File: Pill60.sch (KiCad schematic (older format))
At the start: 139 parts, among them J1 OLED, SW1 Rotary_Encoder_Switch, U1 ChinaBluePill

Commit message: gerber
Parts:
- added H1, H2, H3, H4, H5, H6, H7: Hole, MountingHole:MountingHole_2.2mm_M2, symbol keebio:Hole
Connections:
- no-connect marks 0 -> 11
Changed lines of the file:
@@
-$EndComp
-$Comp
-L MX_Alps_Hybrid:MX-NoLED MXBSPC1
-U 1 1 5F3D669D
-P 9250 3500
-F 0 "MXBSPC1" H 9283 3723 60  0000 C CNN
-F 1 "MX-NoLED" H 9283 3649 20  0000 C CNN
-F 2 "MX_Only:MXOnly-1U-Hotswap-Antishear" H 8625 3475 60  0001 C CNN
-F 3 "" H 8625 3475 60  0001 C CNN
-	1    9250 3500
-	1    0    0    -1
 $EndComp
 $Comp
@@
 $EndComp
 $Comp
-L MX_Alps_Hybrid:MX-NoLED 15MXBSLSH1
-U 1 1 5F53A61E
-P 9250 4450
-F 0 "15MXBSLSH1" H 9283 4673 60  0000 C CNN
-F 1 "MX-NoLED" H 9283 4599 20  0000 C CNN
-F 2 "MX_Only:MXOnly-1.5U-Hotswap-AntiShear" H 8625 4425 60  0001 C CNN
-F 3 "" H 8625 4425 60  0001 C CNN
-	1    9250 4450
-	1    0    0    -1
-$EndComp
-$Comp
 L MX_Alps_Hybrid:MX-NoLED MXFN1
 U 1 1 5F53A62A
@@
 $EndComp
 $Comp
-L MX_Alps_Hybrid:MX-NoLED MXDEL1
-U 1 1 5F53A636
-P 9250 5200
-F 0 "MXDEL1" H 9283 5423 60  0000 C CNN
-F 1 "MX-NoLED" H 9283 5349 20  0000 C CNN
-F 2 "MX_Only:MXOnly-1U-Hotswap-Antishear" H 8625 5175 60  0001 C CNN
-F 3 "" H 8625 5175 60  0001 C CNN
-	1    9250 5200
-	1    0    0    -1
-$EndComp
-$Comp
 L MX_Alps_Hybrid:MX-NoLED 15MXLCTRL1
 U 1 1 5F544C28
@@
 $EndComp
 $Comp
-L Diode:1N4148W D58
-U 1 1 5F4616B7
-P 9200 3800
-F 0 "D58" V 9246 3720 50  0000 R CNN
-F 1 "1N4148W" V 9155 3720 50  0000 R CNN
-F 2 "Diode_SMD:D_SOD-123" H 9200 3625 50  0001 C CNN
-F 3 "https://www.vishay.com/docs/85748/1n4148w.pdf" H 9200 3800 50  0001 C CNN
-	1    9200 3800
-	0    -1   -1   0
-$EndComp
-$Comp
 L Diode:1N4148W D7
 U 1 1 5F47AC29
@@
 $EndComp
 $Comp
-L Diode:1N4148W D59
-U 1 1 5F47AC77
-P 9200 4750
-F 0 "D59" V 9246 4670 50  0000 R CNN
-F 1 "1N4148W" V 9155 4670 50  0000 R CNN
-F 2 "Diode_SMD:D_SOD-123" H 9200 4575 50  0001 C CNN
-F 3 "https://www.vishay.com/docs/85748/1n4148w.pdf" H 9200 4750 50  0001 C CNN
-	1    9200 4750
-	0    -1   -1   0
-$EndComp
-$Comp
 L Diode:1N4148W D8
 U 1 1 5F48F64C
@@
 $EndComp
 $Comp
-L Diode:1N4148W D63
-U 1 1 5F48F694
-P 9200 5500
-F 0 "D63" V 9246 5420 50  0000 R CNN
-F 1 "1N4148W" V 9155 5420 50  0000 R CNN
-F 2 "Diode_SMD:D_SOD-123" H 9200 5325 50  0001 C CNN
-F 3 "https://www.vishay.com/docs/85748/1n4148w.pdf" H 9200 5500 50  0001 C CNN
-	1    9200 5500
-	0    -1   -1   0
-$EndComp
-$Comp
 L Diode:1N4148W D60
 U 1 1 5F48F69A
@@
 Wire Wire Line
 	8800 6800 8800 7600
-Wire Wire Line
-	9400 3000 9400 3450
-Connection ~ 9400 3450
-Wire Wire Line
-	9400 3450 9400 4400
-Connection ~ 9400 4400
 Connection ~ 9400 6800
 Wire Wire Line
 	9400 6800 9400 7600
-Wire Wire Line
-	9200 3950 8600 3950
 Connection ~ 2600 3950
 Wire Wire Line
@@
 Wire Wire Line
 	8050 3950 7500 3950
-Connection ~ 8600 3950
 Wire Wire Line
 	8600 3950 8050 3950
@@
 Wire Wire Line
 	8050 4900 8600 4900
-Connection ~ 8600 4900
-Wire Wire Line
-	8600 4900 9200 4900
 Wire Wire Line
 	1500 5650 2600 5650
@@
 Wire Wire Line
 	8050 5650 8600 5650
-Connection ~ 8600 5650
-Wire Wire Line
-	8600 5650 9200 5650
 Wire Wire Line
 	1500 6450 2600 6450
@@
 	8800 5950 8800 6800
 Connection ~ 8800 5950
-Connection ~ 9400 5150
 Wire Wire Line
 	9200 7300 8600 7300
@@
 Text GLabel 5550 1750 2    50   Input ~ 0
 SWE2
-Text GLabel 4200 6700 0    50   Input ~ 0
-SWE1
-Text GLabel 4000 7000 1    50   Input ~ 0
-SWE2
-$Comp
-L Diode:1N4148W D64
-U 1 1 5F3FC91B
-P 4000 7150
-F 0 "D64" V 4046 7070 50  0000 R CNN
-F 1 "1N4148W" V 3955 7070 50  0000 R CNN
-F 2 "Diode_SMD:D_SOD-123" H 4000 6975 50  0001 C CNN
-F 3 "https://www.vishay.com/docs/85748/1n4148w.pdf" H 4000 7150 50  0001 C CNN
-	1    4000 7150
-	0    -1   -1   0
-$EndComp
-Wire Wire Line
-	9400 4400 9400 5150
-Wire Wire Line
-	3500 7300 4000 7300
 Text GLabel 11700 2000 0    50   Input ~ 0
 COL4
@@
 Text GLabel 13100 2400 2    50   Input ~ 0
 ROW0
-Connection ~ 4000 7300
-Wire Wire Line
-	4000 7300 5500 7300
-Wire Wire Line
-	4200 5950 4200 6700
-Connection ~ 4200 5950
-Wire Wire Line
-	9400 5150 9400 6800
 $Comp
 L china_bluepill:ChinaBluePill U1
@@
 Text GLabel 13100 2500 2    50   Input ~ 0
 COL0
+Connection ~ 4200 5950
+Wire Wire Line
+	4200 5950 4200 6700
+Connection ~ 4000 7300
+Wire Wire Line
+	4000 7300 5500 7300
+Wire Wire Line
+	3500 7300 4000 7300
+$Comp
+L Diode:1N4148W D64
+U 1 1 5F3FC91B
+P 4000 7150
+F 0 "D64" V 4046 7070 50  0000 R CNN
+F 1 "1N4148W" V 3955 7070 50  0000 R CNN
+F 2 "Diode_SMD:D_SOD-123" H 4000 6975 50  0001 C CNN
+F 3 "https://www.vishay.com/docs/85748/1n4148w.pdf" H 4000 7150 50  0001 C CNN
+	1    4000 7150
+	0    -1   -1   0
+$EndComp
+Text GLabel 4000 7000 1    50   Input ~ 0
+SWE2
+Text GLabel 4200 6700 0    50   Input ~ 0
+SWE1
+Wire Wire Line
+	9400 4400 9400 5150
+Connection ~ 9400 5150
+Connection ~ 8600 5650
+Connection ~ 8600 4900
+Connection ~ 8600 3950
+Connection ~ 9400 4400
+Connection ~ 9400 3450
+Wire Wire Line
+	9400 3000 9400 3450
+Wire Wire Line
+	9400 5150 9400 6800
+Wire Wire Line
+	9400 3450 9400 4400
+Wire Wire Line
+	8600 5650 9200 5650
+Wire Wire Line
+	8600 4900 9200 4900
+Wire Wire Line
+	9200 3950 8600 3950
+$Comp
+L Diode:1N4148W D63
+U 1 1 5F48F694
+P 9200 5500
+F 0 "D63" V 9246 5420 50  0000 R CNN
+F 1 "1N4148W" V 9155 5420 50  0000 R CNN
+F 2 "Diode_SMD:D_SOD-123" H 9200 5325 50  0001 C CNN
+F 3 "https://www.vishay.com/docs/85748/1n4148w.pdf" H 9200 5500 50  0001 C CNN
+	1    9200 5500
+	0    -1   -1   0
+$EndComp
+$Comp
+L Diode:1N4148W D59
+U 1 1 5F47AC77
+P 9200 4750
+F 0 "D59" V 9246 4670 50  0000 R CNN
+F 1 "1N4148W" V 9155 4670 50  0000 R CNN
+F 2 "Diode_SMD:D_SOD-123" H 9200 4575 50  0001 C CNN
+F 3 "https://www.vishay.com/docs/85748/1n4148w.pdf" H 9200 4750 50  0001 C CNN
+	1    9200 4750
+	0    -1   -1   0
+$EndComp
+$Comp
+L Diode:1N4148W D58
+U 1 1 5F4616B7
+P 9200 3800
+F 0 "D58" V 9246 3720 50  0000 R CNN
+F 1 "1N4148W" V 9155 3720 50  0000 R CNN
+F 2 "Diode_SMD:D_SOD-123" H 9200 3625 50  0001 C CNN
+F 3 "https://www.vishay.com/docs/85748/1n4148w.pdf" H 9200 3800 50  0001 C CNN
+	1    9200 3800
+	0    -1   -1   0
+$EndComp
+$Comp
+L MX_Alps_Hybrid:MX-NoLED MXDEL1
+U 1 1 5F53A636
+P 9250 5200
+F 0 "MXDEL1" H 9283 5423 60  0000 C CNN
+F 1 "MX-NoLED" H 9283 5349 20  0000 C CNN
+F 2 "MX_Only:MXOnly-1U-Hotswap-Antishear" H 8625 5175 60  0001 C CNN
+F 3 "" H 8625 5175 60  0001 C CNN
+	1    9250 5200
+	1    0    0    -1
+$EndComp
+$Comp
+L MX_Alps_Hybrid:MX-NoLED 15MXBSLSH1
+U 1 1 5F53A61E
+P 9250 4450
+F 0 "15MXBSLSH1" H 9283 4673 60  0000 C CNN
+F 1 "MX-NoLED" H 9283 4599 20  0000 C CNN
+F 2 "MX_Only:MXOnly-1.5U-Hotswap-AntiShear" H 8625 4425 60  0001 C CNN
+F 3 "" H 8625 4425 60  0001 C CNN
+	1    9250 4450
+	1    0    0    -1
+$EndComp
+$Comp
+L MX_Alps_Hybrid:MX-NoLED MXBSPC1
+U 1 1 5F3D669D
+P 9250 3500
+F 0 "MXBSPC1" H 9283 3723 60  0000 C CNN
+F 1 "MX-NoLED" H 9283 3649 20  0000 C CNN
+F 2 "MX_Only:MXOnly-1U-Hotswap-Antishear" H 8625 3475 60  0001 C CNN
+F 3 "" H 8625 3475 60  0001 C CNN
+	1    9250 3500
+	1    0    0    -1
+$EndComp
+$Comp
+L keebio:Hole H1
+U 1 1 5F48208A
+P 11150 5500
+F 0 "H1" H 11336 5553 60  0000 L CNN
+F 1 "Hole" H 11336 5447 60  0000 L CNN
+F 2 "MountingHole:MountingHole_2.2mm_M2" H 11150 5500 60  0001 C CNN
+F 3 "" H 11150 5500 60  0001 C CNN
+	1    11150 5500
+	1    0    0    -1
+$EndComp
+$Comp
+L keebio:Hole H2
+U 1 1 5F4826F6
+P 11800 5500
+F 0 "H2" H 11986 5553 60  0000 L CNN
+F 1 "Hole" H 11986 5447 60  0000 L CNN
+F 2 "MountingHole:MountingHole_2.2mm_M2" H 11800 5500 60  0001 C CNN
+F 3 "" H 11800 5500 60  0001 C CNN
+	1    11800 5500
+	1    0    0    -1
+$EndComp
+$Comp
+L keebio:Hole H3
+U 1 1 5F482881
+P 12400 5500
+F 0 "H3" H 12586 5553 60  0000 L CNN
+F 1 "Hole" H 12586 5447 60  0000 L CNN
+F 2 "MountingHole:MountingHole_2.2mm_M2" H 12400 5500 60  0001 C CNN
+F 3 "" H 12400 5500 60  0001 C CNN
+	1    12400 5500
+	1    0    0    -1
+$EndComp
+$Comp
+L keebio:Hole H4
+U 1 1 5F482A97
+P 12950 5500
+F 0 "H4" H 13136 5553 60  0000 L CNN
+F 1 "Hole" H 13136 5447 60  0000 L CNN
+F 2 "MountingHole:MountingHole_2.2mm_M2" H 12950 5500 60  0001 C CNN
+F 3 "" H 12950 5500 60  0001 C CNN
+	1    12950 5500
+	1    0    0    -1
+$EndComp
+$Comp
+L keebio:Hole H5
+U 1 1 5F482CBA
+P 13500 5500
+F 0 "H5" H 13686 5553 60  0000 L CNN
+F 1 "Hole" H 13686 5447 60  0000 L CNN
+F 2 "MountingHole:MountingHole_2.2mm_M2" H 13500 5500 60  0001 C CNN
+F 3 "" H 13500 5500 60  0001 C CNN
+	1    13500 5500
+	1    0    0    -1
+$EndComp
+$Comp
+L keebio:Hole H6
+U 1 1 5F482E8A
+P 14050 5500
+F 0 "H6" H 14236 5553 60  0000 L CNN
+F 1 "Hole" H 14236 5447 60  0000 L CNN
+F 2 "MountingHole:MountingHole_2.2mm_M2" H 14050 5500 60  0001 C CNN
+F 3 "" H 14050 5500 60  0001 C CNN
+	1    14050 5500
+	1    0    0    -1
+$EndComp
+$Comp
+L keebio:Hole H7
+U 1 1 5F483003
+P 14650 5500
+F 0 "H7" H 14836 5553 60  0000 L CNN
+F 1 "Hole" H 14836 5447 60  0000 L CNN
+F 2 "MountingHole:MountingHole_2.2mm_M2" H 14650 5500 60  0001 C CNN
+F 3 "" H 14650 5500 60  0001 C CNN
+	1    14650 5500
+	1    0    0    -1
+$EndComp
+NoConn ~ 11700 2800
+NoConn ~ 11700 2900
+NoConn ~ 11700 3000
+NoConn ~ 11700 3100
+NoConn ~ 11700 3400
+NoConn ~ 11700 3500
+NoConn ~ 13100 3300
+NoConn ~ 13100 3400
+NoConn ~ 13100 3500
+NoConn ~ 13100 3600
+NoConn ~ 13100 3700
 $EndSCHEMATC

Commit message: add underglow
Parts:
- added L0, L1, L10, L11, L12, L13, L2, L3, L4, L5, L6, L7, L8, L9: SK6812MINI, LED_SMD:LED_SK6812MINI_PLCC4_3.5x3.5mm_P1.75mm, symbol LED:SK6812MINI
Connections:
- net +5V: now also L0.4 (VDD), L1.4 (VDD), L10.4 (VDD), L11.4 (VDD), L12.4 (VDD), L13.4 (VDD), L2.4 (VDD), L3.4 (VDD), L4.4 (VDD), L5.4 (VDD), L6.4 (VDD), L7.4 (VDD), L8.4 (VDD), L9.4 (VDD)
- net GND: now also L0.2 (VSS), L1.2 (VSS), L10.2 (VSS), L11.2 (VSS), L12.2 (VSS), L13.2 (VSS), L2.2 (VSS), L3.2 (VSS), L4.2 (VSS), L5.2 (VSS), L6.2 (VSS), L7.2 (VSS), L8.2 (VSS), L9.2 (VSS)
- net LED: now reaches U1.PA9
- net LED: now also L0.3 (DIN)
- new net: L0.1 (DOUT), L1.3 (DIN)
- new net: L1.1 (DOUT), L2.3 (DIN)
- new net: L2.1 (DOUT), L3.3 (DIN)
- new net: L3.1 (DOUT), L4.3 (DIN)
- new net: L7.1 (DOUT), L8.3 (DIN)
- new net: L6.1 (DOUT), L7.3 (DIN)
- new net: L5.1 (DOUT), L6.3 (DIN)
- new net: L4.1 (DOUT), L5.3 (DIN)
- new net: L12.1 (DOUT), L13.3 (DIN)
- new net: L11.1 (DOUT), L12.3 (DIN)
- new net: L10.3 (DIN), L9.1 (DOUT)
- new net: L8.1 (DOUT), L9.3 (DIN)
- new net: L10.1 (DOUT), L11.3 (DIN)
- no-connect marks 11 -> 10
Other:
- moved on the sheet: H1, H2, H3, H4, H5, H6, H7

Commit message: Fix wires and make stuff better
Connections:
- net COL0: now also U1.PB7; no longer U1.PB6
- net COL1: now also U1.PB8; no longer U1.PB7
- net COL2: now also U1.PB9; no longer U1.PB8
- net COL3: now also U1.PB6; no longer U1.PB9
- net ENCA: now also U1.PB13; no longer U1.PB12
- net ENCB: now also U1.PB12; no longer U1.PB13
- net ROW0: now also U1.PB4; no longer U1.PB5
- net ROW1: now also U1.PB3; no longer U1.PB4
- net ROW2: now also U1.PA15; no longer U1.PB3
- net ROW3: now also U1.PA12; no longer U1.PA15
- net ROW4: now also U1.PB5; no longer U1.PA12
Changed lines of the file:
@@
 Text GLabel 4950 1750 0    50   Input ~ 0
 ENCB
+Text GLabel 13100 3200 2    50   Input ~ 0
+ENCA
 Text GLabel 13100 3100 2    50   Input ~ 0
-ENCA
-Text GLabel 13100 3200 2    50   Input ~ 0
 ENCB
 $Comp
@@
 	0    -1   -1   0
 $EndComp
+Text GLabel 13100 2400 2    50   Input ~ 0
+ROW4
 Text GLabel 11700 3200 0    50   Input ~ 0
-ROW4
+ROW3
 Text GLabel 11700 3300 0    50   Input ~ 0
-ROW3
+ROW2
 Text GLabel 13100 2200 2    50   Input ~ 0
-ROW2
-Text GLabel 13100 2300 2    50   Input ~ 0
 ROW1
 $Comp
@@
 	1    0    0    -1
 $EndComp
+Text GLabel 13100 2500 2    50   Input ~ 0
+COL3
 Text GLabel 13100 2800 2    50   Input ~ 0
-COL3
+COL2
 Text GLabel 13100 2700 2    50   Input ~ 0
-COL2
-Text GLabel 13100 2600 2    50   Input ~ 0
 COL1
 Connection ~ 4200 5950
@@
 NoConn ~ 13100 3600
 NoConn ~ 13100 3700
-Text GLabel 13100 2500 2    50   Input ~ 0
+Text GLabel 13100 2600 2    50   Input ~ 0
 COL0
-Text GLabel 13100 2400 2    50   Input ~ 0
+Text GLabel 13100 2300 2    50   Input ~ 0
 ROW0
 Text GLabel 11700 2900 0    50   Input ~ 0

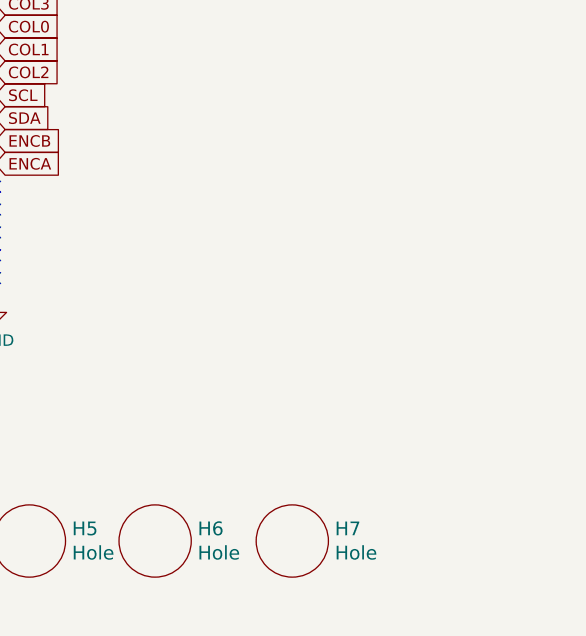
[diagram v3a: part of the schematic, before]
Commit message: added more holes for plate and pcb mounting
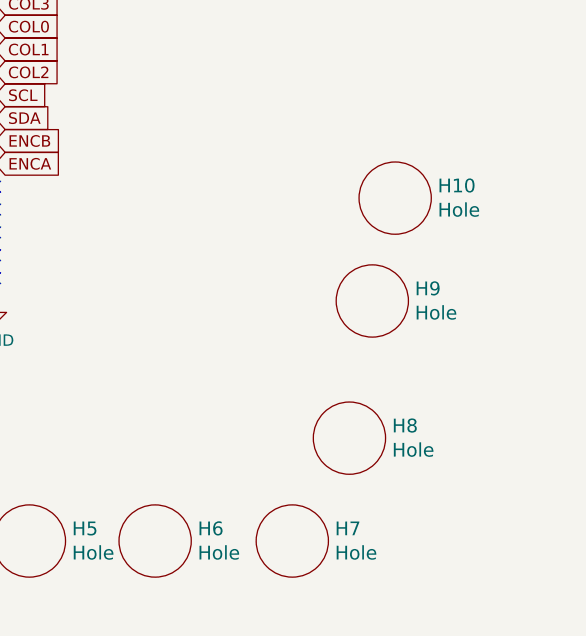
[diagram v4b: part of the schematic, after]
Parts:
- added H10, H8, H9: Hole, MountingHole:MountingHole_2.2mm_M2, symbol keebio:Hole
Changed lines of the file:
@@
 Wire Wire Line
 	10300 8150 13300 8150
+$Comp
+L keebio:Hole H8
+U 1 1 5F429E69
+P 14650 4400
+F 0 "H8" H 14836 4453 60  0000 L CNN
+F 1 "Hole" H 14836 4347 60  0000 L CNN
+F 2 "MountingHole:MountingHole_2.2mm_M2" H 14650 4400 60  0001 C CNN
+F 3 "" H 14650 4400 60  0001 C CNN
+	1    14650 4400
+	1    0    0    -1
+$EndComp
+$Comp
+L keebio:Hole H9
+U 1 1 5F42A107
+P 14750 3800
+F 0 "H9" H 14936 3853 60  0000 L CNN
+F 1 "Hole" H 14936 3747 60  0000 L CNN
+F 2 "MountingHole:MountingHole_2.2mm_M2" H 14750 3800 60  0001 C CNN
+F 3 "" H 14750 3800 60  0001 C CNN
+	1    14750 3800
+	1    0    0    -1
+$EndComp
+$Comp
+L keebio:Hole H10
+U 1 1 5F42A374
+P 14850 3350
+F 0 "H10" H 15036 3403 60  0000 L CNN
+F 1 "Hole" H 15036 3297 60  0000 L CNN
+F 2 "MountingHole:MountingHole_2.2mm_M2" H 14850 3350 60  0001 C CNN
+F 3 "" H 14850 3350 60  0001 C CNN
+	1    14850 3350
+	1    0    0    -1
+$EndComp
 $EndSCHEMATC

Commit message: Sneaky footprint
offset pin holes for bluepill, might or might not work
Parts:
- U1: footprint chinabluepill:ChinaBluePill -> chinabluepill:ChinaBluePill_SneakyFootprint
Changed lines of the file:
@@
 F 0 "U1" H 12400 3365 50  0000 C CNN
 F 1 "ChinaBluePill" H 12400 3274 50  0000 C CNN
-F 2 "chinabluepill:ChinaBluePill" H 12400 2550 50  0001 C CNN
+F 2 "chinabluepill:ChinaBluePill_SneakyFootprint" H 12400 2550 50  0001 C CNN
 F 3 "" H 12400 2550 50  0001 C CNN
 	1    12400 2550

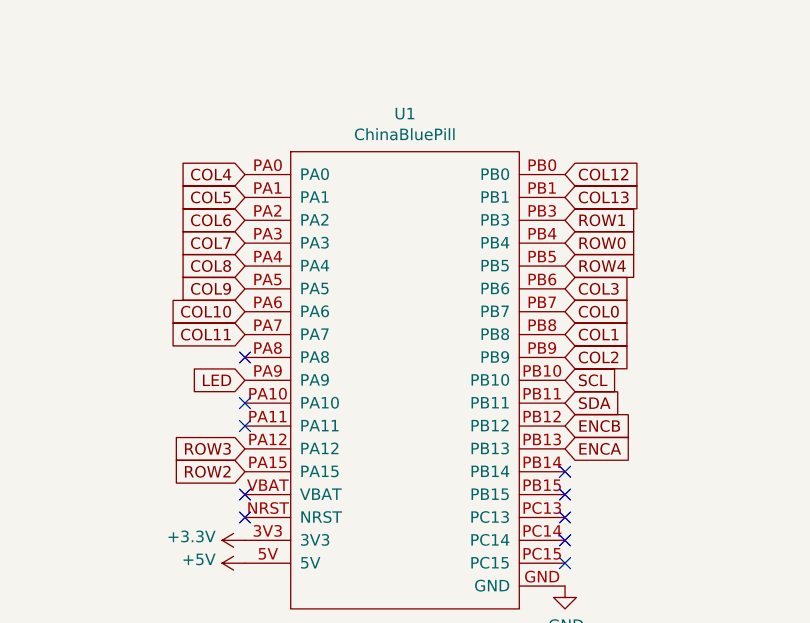
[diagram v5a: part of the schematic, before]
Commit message: added support for blackpill
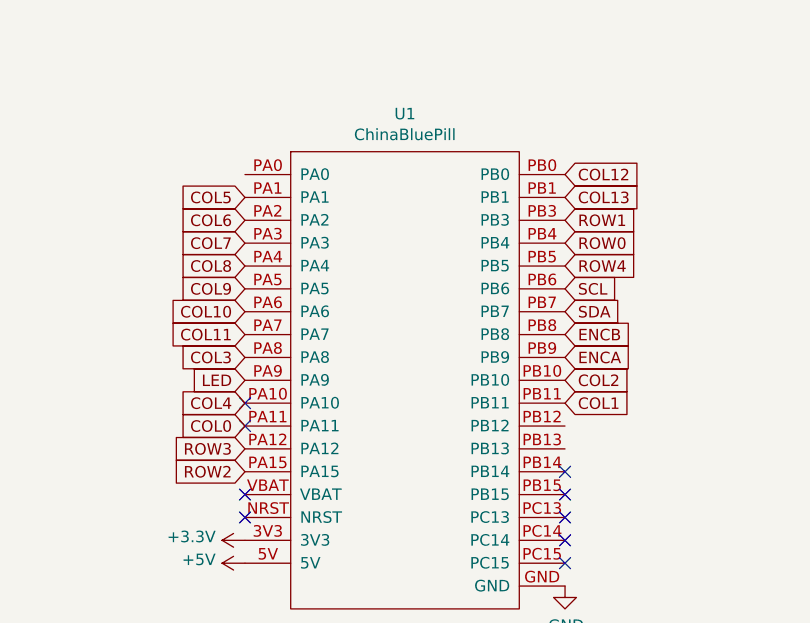
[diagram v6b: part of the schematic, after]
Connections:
- net COL0: now also U1.PA11; no longer U1.PB7
- net COL1: now also U1.PB11; no longer U1.PB8
- net COL2: now also U1.PB10; no longer U1.PB9
- net COL3: now also U1.PA8; no longer U1.PB6
- net COL4: now also U1.PA10; no longer U1.PA0
- net ENCA: now also U1.PB9; no longer U1.PB13
- net ENCB: now also U1.PB8; no longer U1.PB12
- net SCL: now also U1.PB6; no longer U1.PB10
- net SDA: now also U1.PB7; no longer U1.PB11
- no-connect marks 10 -> 9
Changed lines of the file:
@@
 	1    0    0    -1
 $EndComp
-Text GLabel 13100 3000 2    50   Input ~ 0
+Text GLabel 13100 2600 2    50   Input ~ 0
 SDA
-Text GLabel 13100 2900 2    50   Input ~ 0
+Text GLabel 13100 2500 2    50   Input ~ 0
 SCL
 $Comp
@@
 Text GLabel 5550 1750 2    50   Input ~ 0
 SWE2
-Text GLabel 11700 2000 0    50   Input ~ 0
+Text GLabel 11700 3000 0    50   Input ~ 0
 COL4
 Text GLabel 11700 2100 0    50   Input ~ 0
@@
 Text GLabel 4950 1750 0    50   Input ~ 0
 ENCB
-Text GLabel 13100 3200 2    50   Input ~ 0
+Text GLabel 13100 2800 2    50   Input ~ 0
 ENCA
-Text GLabel 13100 3100 2    50   Input ~ 0
+Text GLabel 13100 2700 2    50   Input ~ 0
 ENCB
 $Comp
@@
 	1    0    0    -1
 $EndComp
-Text GLabel 13100 2500 2    50   Input ~ 0
+Text GLabel 11700 2800 0    50   Input ~ 0
 COL3
-Text GLabel 13100 2800 2    50   Input ~ 0
+Text GLabel 13100 2900 2    50   Input ~ 0
 COL2
-Text GLabel 13100 2700 2    50   Input ~ 0
+Text GLabel 13100 3000 2    50   Input ~ 0
 COL1
 Connection ~ 4200 5950
@@
 	1    0    0    -1
 $EndComp
-NoConn ~ 11700 2800
 NoConn ~ 11700 3000
 NoConn ~ 11700 3100
@@
 NoConn ~ 13100 3600
 NoConn ~ 13100 3700
-Text GLabel 13100 2600 2    50   Input ~ 0
+Text GLabel 11700 3100 0    50   Input ~ 0
 COL0
 Text GLabel 13100 2300 2    50   Input ~ 0

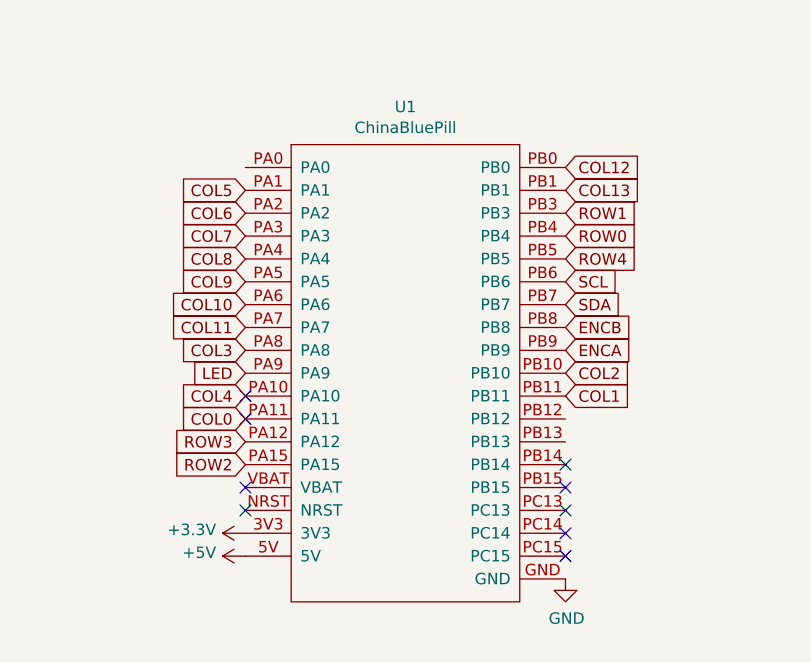
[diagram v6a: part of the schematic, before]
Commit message: changed pin diagram to avoid bad pin
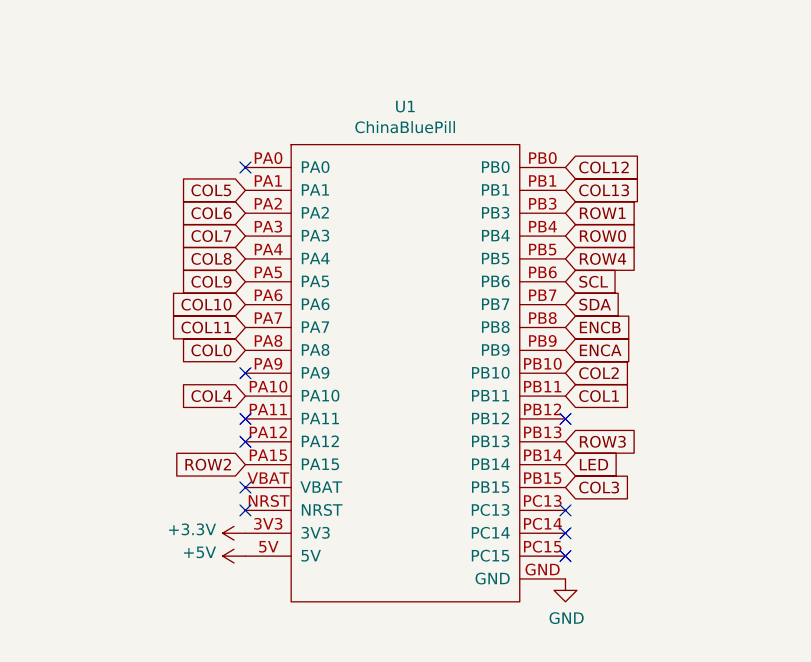
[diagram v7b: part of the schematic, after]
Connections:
- net COL0: now also U1.PA8; no longer U1.PA11
- net COL3: now also U1.PB15; no longer U1.PA8
- net LED: now also U1.PB14; no longer U1.PA9
- net ROW3: now also U1.PB13; no longer U1.PA12
- no-connect marks 9 -> 10
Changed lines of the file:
@@
 Text GLabel 13100 2400 2    50   Input ~ 0
 ROW4
-Text GLabel 11700 3200 0    50   Input ~ 0
+Text GLabel 13100 3200 2    50   Input ~ 0
 ROW3
 Text GLabel 11700 3300 0    50   Input ~ 0
@@
 	1    0    0    -1
 $EndComp
-Text GLabel 11700 2800 0    50   Input ~ 0
+Text GLabel 13100 3400 2    50   Input ~ 0
 COL3
 Text GLabel 13100 2900 2    50   Input ~ 0
@@
 	1    0    0    -1
 $EndComp
-NoConn ~ 11700 3000
-NoConn ~ 11700 3100
 NoConn ~ 11700 3400
 NoConn ~ 11700 3500
-NoConn ~ 13100 3300
-NoConn ~ 13100 3400
 NoConn ~ 13100 3500
 NoConn ~ 13100 3600
 NoConn ~ 13100 3700
-Text GLabel 11700 3100 0    50   Input ~ 0
+Text GLabel 11700 2800 0    50   Input ~ 0
 COL0
 Text GLabel 13100 2300 2    50   Input ~ 0
 ROW0
-Text GLabel 11700 2900 0    50   Input ~ 0
+Text GLabel 13100 3300 2    50   Input ~ 0
 LED
 $Comp
@@
 	1    0    0    -1
 $EndComp
+NoConn ~ 11700 2000
+NoConn ~ 13100 3100
+NoConn ~ 11700 2900
+NoConn ~ 11700 3100
+NoConn ~ 11700 3200
 $EndSCHEMATC
